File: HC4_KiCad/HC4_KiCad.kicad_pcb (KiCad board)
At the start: 2 copper layers, 150.4 x 175 mm, 168 parts, among them IC1 RAM, IC10 74HC4002, IC11 74HC161, IC12 74HC377, IC13 74HC161, IC14 74HC161, IC15 74HC161, IC16 74HC257, IC17 74HC257, IC18 74HC32, IC19 74HC74, IC2 ROM, IC20 74HC00, IC21 74HC4053, IC22 74HC04, IC23 74HC151, IC24 74HC14, IC3 74HC153, IC4 74HC153, IC5 74HC153, IC6 74HC153, IC7 74HC283, IC8 74HC257, IC9 74HC244, J1 Power, J2 CE, J3 Expantion_Connector, SW1 SW_SPDT, SW2 Bus_Open, SW3 SW_Push, SW4 SW_Push, SW5 SW_SPDT

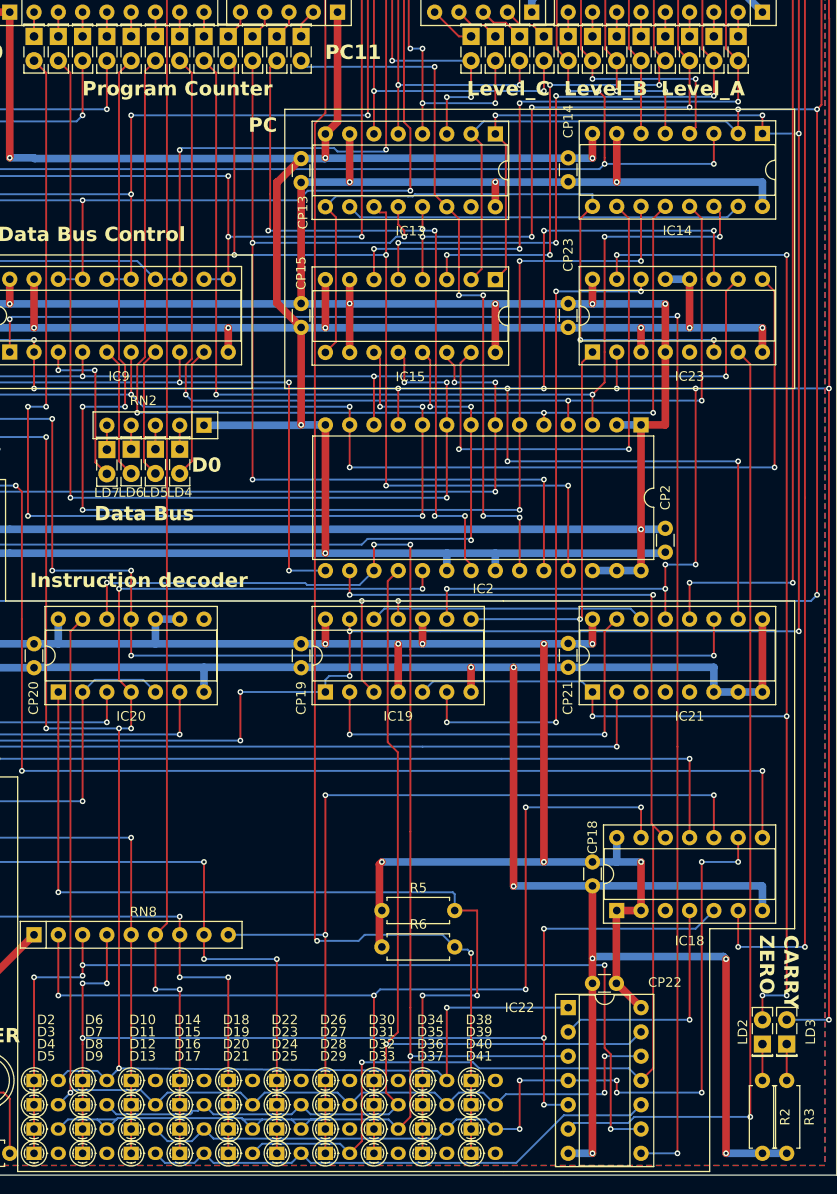
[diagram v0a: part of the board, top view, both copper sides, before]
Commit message: メモリーを外に出した　ガーバーを修正した
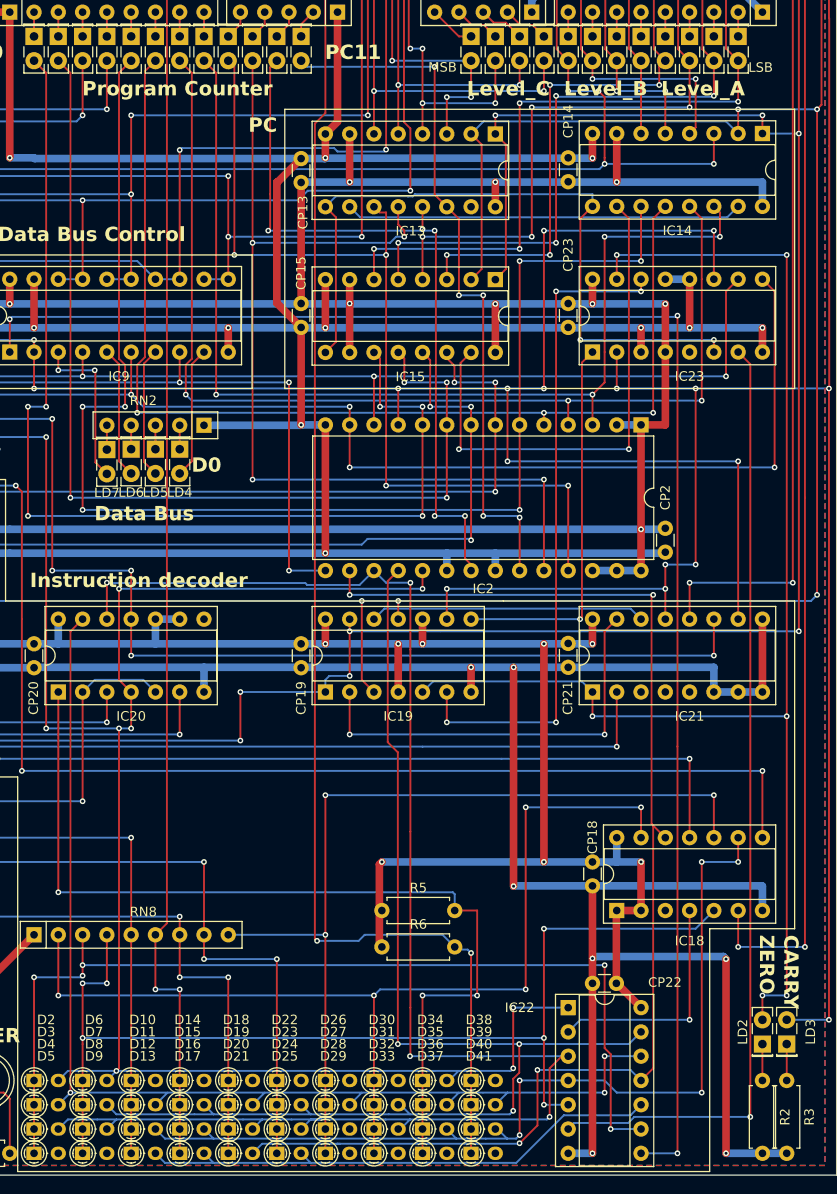
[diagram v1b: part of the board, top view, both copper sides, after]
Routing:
- net /Address BUS/Instruction_6: track 118.1 -> 131.2 mm, vias 1 -> 3
- net /Address BUS/Instruction_5: track 163.7 -> 169.4 mm
- net /Instruction Decoder/~{i6}: track 120.8 -> 124.3 mm
- net /Address BUS/Instruction_4: track 138.6 -> 136.0 mm, vias 3 -> 4
- net /Instruction Decoder/~{i5}: track 96.7 -> 98.9 mm, vias 7 -> 5
- net /Instruction Decoder/~{i4}: track 55.4 -> 56.6 mm
- net /Address BUS/Instruction_7: track 300.0 -> 300.9 mm, vias 11 -> 12
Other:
- board text added: "LSB"
- board text added: "MSB"

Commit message: 回路の改良　試験は明日やる
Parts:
- removed the IC20 at (94.0, 147.3)
- removed the RN1 at (57.2, 109.2)
- added IC21: 74HC00, Package_DIP:DIP-14_W7.62mm_Socket, F.Cu at (94.0, 147.3)
- added J2: ~{CE}_EXT, Connector_PinHeader_2.54mm:PinHeader_1x01_P2.54mm_Vertical, F.Cu at (243.3, 84.7)
- added JP1: RAM_Select, Connector_PinHeader_2.54mm:PinHeader_1x03_P2.54mm_Vertical, F.Cu at (238.6, 81.5)
- added RN2: 10k, Resistor_THT:R_Array_SIP9, F.Cu at (202.6, 84.5)
- added RN8: 1k, Resistor_THT:R_Array_SIP5, F.Cu at (252.1, 115.8)
- added SW1: SW_SPDT_312, Button_Switch_THT:SW_Slide-03_Wuerth-WS-SLTV_10x2.5x6.4_P2.54mm, F.Cu at (242.1, 77.2)
- D10, D11, D12, D13, D14, D15, D16, D17, D18, D19, D2, D20, D21, D22, D23, D24, D25, D26, D27, D28, D29, D3, D30, D31, D32, D33, D34, D35, D36, D37, D38, D39, D4, D40, D41, D5, D6, D7, D8, D9: footprint Library:DO-35_horizontal_anodeup_Smallhole -> Diode_SMD:D_SOD-323_HandSoldering
- IC1: value RAM -> KM62256CLP
- IC2: footprint Package_DIP:DIP-28_W15.24mm -> Socket:DIP_Socket-28_W11.9_W12.7_W15.24_W17.78_W18.5_3M_228-1277-00-0602J
- LD1: footprint LED_THT:LED_D5.0mm -> LED_THT:LED_Rectangular_W5.0mm_H2.0mm
- LD40, LD41: value D -> LED; footprint LED_THT:LED_D5.0mm -> LED_THT:LED_Rectangular_W5.0mm_H2.0mm
- RN3: value R_Network04_Split -> 1k; footprint Resistor_THT:R_Array_SIP5 -> Resistor_THT:R_Array_SIP9
- RN4: value R_Network08_Split -> 1k
- RN5: footprint Resistor_THT:R_Array_SIP5 -> Resistor_THT:R_Array_SIP9
- RN7: value 1k -> 10k
- moved RN7 229.4 mm to (252.1, 90.0)
- moved CP17 216.6 mm to (274.2, -4.97), turned to 0 degrees
- moved LD32 211.6 mm to (241.2, -4.71), turned to 0 degrees
- moved LD33 208.4 mm to (241.2, -1.04), turned to 0 degrees
- moved LD34 205.3 mm to (241.2, 2.62), turned to 0 degrees
- moved LD35 202.3 mm to (241.2, 6.29), turned to 0 degrees
- moved IC17 199.8 mm to (259.6, -0.07), turned to 0 degrees
- moved LD36 199.3 mm to (241.2, 9.96), turned to 0 degrees
- moved CP1 198.7 mm to (242.5, 80.8), turned to 0 degrees
- moved LD37 196.4 mm to (241.2, 13.6), turned to 0 degrees
- moved LD38 193.6 mm to (241.2, 17.3), turned to 0 degrees
- moved IC16 191.9 mm to (247.9, -0.07), turned to 0 degrees
- moved R4 191.8 mm to (258.9, 21.9), turned to 0 degrees
- moved LD39 190.8 mm to (241.2, 21.0), turned to 0 degrees
- moved LD31 185.4 mm to (276.8, 73.4), turned to 0 degrees
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- renumbered IC19 to IC18, IC18 to IC19, IC22 to IC20, IC21 to IC22, R12 to R10, R15 to R11, R9 to R7, R10 to R8, R11 to R9, RN2 to RN1
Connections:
- net /Data BUS/Stack0 renamed /Data BUS/Databus0
- net /Data BUS/Stack1 renamed /Data BUS/Databus1
- net /Data BUS/Stack2 renamed /Data BUS/Databus2
- net /Data BUS/Stack3 renamed /Data BUS/Databus3
- net /Instruction Decoder/ALU_~{Eb} renamed /Instruction Decoder/~{Carry_EN}
- D10 pad 1: /Address BUS/MEMMode -> unconnected-(D10-K-Pad1)
- D10 pad 2: unconnected-(D10-A-Pad2) -> /Address BUS/MEMMode
- D11 pad 1: /Address BUS/MEMMode -> /Instruction Decoder/~{i6}
- D11 pad 2: /Instruction Decoder/~{i6} -> /Address BUS/MEMMode
- D12 pad 1: /Address BUS/MEMMode -> /Instruction Decoder/~{i5}
- D12 pad 2: /Instruction Decoder/~{i5} -> /Address BUS/MEMMode
- D13 pad 1: /Address BUS/MEMMode -> /Instruction Decoder/~{i4}
- D13 pad 2: /Instruction Decoder/~{i4} -> /Address BUS/MEMMode
- D14 pad 1: /ALU/I0a -> unconnected-(D14-K-Pad1)
- D14 pad 2: unconnected-(D14-A-Pad2) -> /ALU/Carry_IN
- D15 pad 1: /ALU/I0a -> /Address BUS/Instruction_6
- D15 pad 2: /Address BUS/Instruction_6 -> /ALU/Carry_IN
- D16 pad 1: /ALU/I0a -> /Instruction Decoder/~{i5}
- D16 pad 2: /Instruction Decoder/~{i5} -> /ALU/Carry_IN
- D17 pad 1: /ALU/I0a -> /Instruction Decoder/~{i4}
- D17 pad 2: /Instruction Decoder/~{i4} -> /ALU/Carry_IN
- D18 pad 1: Net-(D18-K) -> unconnected-(D18-K-Pad1)
- D18 pad 2: unconnected-(D18-A-Pad2) -> Net-(D18-A)
- D19 pad 1: Net-(D18-K) -> /Instruction Decoder/~{i6}
- D19 pad 2: /Instruction Decoder/~{i6} -> Net-(D18-A)
- D2 pad 1: Net-(D2-K) -> unconnected-(D2-K-Pad1)
- D2 pad 2: /Address BUS/Instruction_7 -> Net-(D2-A)
- D20 pad 1: Net-(D18-K) -> unconnected-(D20-K-Pad1)
- D20 pad 2: /Address BUS/Instruction_5 -> Net-(D18-A)
- D21 pad 1: Net-(D18-K) -> /Address BUS/Instruction_4
- D21 pad 2: /Address BUS/Instruction_4 -> Net-(D18-A)
- D22 pad 1: Net-(D22-K) -> unconnected-(D22-K-Pad1)
- D22 pad 2: unconnected-(D22-A-Pad2) -> Net-(D22-A)
- D23 pad 1: Net-(D22-K) -> /Address BUS/Instruction_6
- D23 pad 2: /Address BUS/Instruction_6 -> Net-(D22-A)
- D24 pad 1: Net-(D22-K) -> /Address BUS/Instruction_5
- D24 pad 2: /Address BUS/Instruction_5 -> Net-(D22-A)
- D25 pad 1: Net-(D22-K) -> /Instruction Decoder/~{i4}
- D25 pad 2: /Instruction Decoder/~{i4} -> Net-(D22-A)
- D26 pad 1: Net-(D26-K) -> unconnected-(D26-K-Pad1)
- D26 pad 2: unconnected-(D26-A-Pad2) -> Net-(D26-A)
- D27 pad 1: Net-(D26-K) -> /Instruction Decoder/~{i6}
- D27 pad 2: /Instruction Decoder/~{i6} -> Net-(D26-A)
- D28 pad 1: Net-(D26-K) -> unconnected-(D28-K-Pad1)
- D28 pad 2: unconnected-(D28-A-Pad2) -> Net-(D26-A)
- D29 pad 1: Net-(D26-K) -> /Address BUS/Instruction_4
- D29 pad 2: /Address BUS/Instruction_4 -> Net-(D26-A)
- D3 pad 1: Net-(D2-K) -> /Instruction Decoder/~{i6}
- D3 pad 2: /Instruction Decoder/~{i6} -> Net-(D2-A)
- D30 pad 1: Net-(D30-K) -> unconnected-(D30-K-Pad1)
- D30 pad 2: unconnected-(D30-A-Pad2) -> Net-(D30-A)
- D31 pad 1: Net-(D30-K) -> /Address BUS/Instruction_6
- D31 pad 2: /Address BUS/Instruction_6 -> Net-(D30-A)
- D32 pad 1: Net-(D30-K) -> /Address BUS/Instruction_5
- D32 pad 2: /Address BUS/Instruction_5 -> Net-(D30-A)
- D33 pad 1: Net-(D30-K) -> unconnected-(D33-K-Pad1)
- D33 pad 2: unconnected-(D33-A-Pad2) -> Net-(D30-A)
- D34 pad 1: /Instruction Decoder/READ -> /Address BUS/Instruction_7
- D34 pad 2: /Address BUS/Instruction_7 -> /Instruction Decoder/READ
- D35 pad 1: /Instruction Decoder/READ -> /Instruction Decoder/~{i6}
- D35 pad 2: /Instruction Decoder/~{i6} -> /Instruction Decoder/READ
- D36 pad 1: /Instruction Decoder/READ -> /Instruction Decoder/~{i5}
- D36 pad 2: /Instruction Decoder/~{i5} -> /Instruction Decoder/READ
- D37 pad 1: /Instruction Decoder/READ -> unconnected-(D37-K-Pad1)
- D37 pad 2: unconnected-(D37-A-Pad2) -> /Instruction Decoder/READ
- D38 pad 1: /Data BUS/Level_C_OE -> unconnected-(D38-K-Pad1)
- D38 pad 2: unconnected-(D38-A-Pad2) -> /Data BUS/Level_C_OE
- D39 pad 1: /Data BUS/Level_C_OE -> /Instruction Decoder/~{i6}
- D39 pad 2: /Instruction Decoder/~{i6} -> /Data BUS/Level_C_OE
- D4 pad 1: Net-(D2-K) -> /Address BUS/Instruction_5
- D4 pad 2: /Address BUS/Instruction_5 -> Net-(D2-A)
- D40 pad 1: /Data BUS/Level_C_OE -> /Instruction Decoder/~{i5}
- D40 pad 2: /Instruction Decoder/~{i5} -> /Data BUS/Level_C_OE
- D41 pad 1: /Data BUS/Level_C_OE -> unconnected-(D41-K-Pad1)
- D41 pad 2: unconnected-(D41-A-Pad2) -> /Data BUS/Level_C_OE
- D5 pad 1: Net-(D2-K) -> unconnected-(D5-K-Pad1)
- D5 pad 2: unconnected-(D5-A-Pad2) -> Net-(D2-A)
- D6 pad 1: Net-(D6-K) -> /Address BUS/Instruction_7
- D6 pad 2: /Address BUS/Instruction_7 -> Net-(D6-A)
- D7 pad 1: Net-(D6-K) -> /Address BUS/Instruction_6
- D7 pad 2: /Address BUS/Instruction_6 -> Net-(D6-A)
- D8 pad 1: Net-(D6-K) -> /Address BUS/Instruction_5
- D8 pad 2: /Address BUS/Instruction_5 -> Net-(D6-A)
- D9 pad 1: Net-(D6-K) -> unconnected-(D9-K-Pad1)
- D9 pad 2: unconnected-(D9-A-Pad2) -> Net-(D6-A)
- IC1 pad 16: Net-(IC1-Q4) -> /Data BUS/Dummy4
- IC1 pad 17: Net-(IC1-Q5) -> /Data BUS/Dummy5
- IC1 pad 18: Net-(IC1-Q6) -> /Data BUS/Dummy6
- IC1 pad 19: Net-(IC1-Q7) -> /Data BUS/Dummy7
- IC10 pad 2: Net-(D18-K) -> Net-(D18-A)
- IC10 pad 3: Net-(D18-K) -> Net-(D18-A)
- IC10 pad 4: Net-(D22-K) -> Net-(D22-A)
- IC10 pad 5: Net-(D22-K) -> Net-(D22-A)
- IC13 pad 11: /Program Counter/PC_8 -> /Program Counter/PC_11
- IC13 pad 12: /Program Counter/PC_9 -> /Program Counter/PC_10
- IC13 pad 13: /Program Counter/PC_10 -> /Program Counter/PC_9
- IC13 pad 14: /Program Counter/PC_11 -> /Program Counter/PC_8
- IC13 pad 3: /Data BUS/Level_C3 -> /Data BUS/Level_C0
- IC13 pad 4: /Data BUS/Level_C2 -> /Data BUS/Level_C1
- IC13 pad 5: /Data BUS/Level_C1 -> /Data BUS/Level_C2
- IC13 pad 6: /Data BUS/Level_C0 -> /Data BUS/Level_C3
- IC14 pad 11: /Program Counter/PC_4 -> /Program Counter/PC_7
- IC14 pad 12: /Program Counter/PC_5 -> /Program Counter/PC_6
- IC14 pad 13: /Program Counter/PC_6 -> /Program Counter/PC_5
- IC14 pad 14: /Program Counter/PC_7 -> /Program Counter/PC_4
- IC14 pad 3: /ALU/ALU_in_B3 -> /ALU/ALU_in_B0
- IC14 pad 4: /ALU/ALU_in_B2 -> /ALU/ALU_in_B1
- IC14 pad 5: /ALU/ALU_in_B1 -> /ALU/ALU_in_B2
- IC14 pad 6: /ALU/ALU_in_B0 -> /ALU/ALU_in_B3
- IC15 pad 11: /Program Counter/PC_0 -> /Program Counter/PC_3
- IC15 pad 12: /Program Counter/PC_1 -> /Program Counter/PC_2
- IC15 pad 13: /Program Counter/PC_2 -> /Program Counter/PC_1
- IC15 pad 14: /Program Counter/PC_3 -> /Program Counter/PC_0
- IC15 pad 3: /ALU/ALU_in_A3 -> /ALU/ALU_in_A0
- IC15 pad 4: /ALU/ALU_in_A2 -> /ALU/ALU_in_A1
- IC15 pad 5: /ALU/ALU_in_A1 -> /ALU/ALU_in_A2
- IC15 pad 6: /ALU/ALU_in_A0 -> /ALU/ALU_in_A3
- IC19 pad 10: Net-(D26-K) -> Net-(D26-A)
- IC19 pad 13: Net-(D30-K) -> Net-(D30-A)
- IC19 pad 5: Net-(D6-K) -> Net-(D6-A)
- IC20 pad 5: Net-(D6-K) -> Net-(D6-A)
- IC20 pad 8: /Data BUS/~{Immediate_OE} -> unconnected-(IC20-Pad8)
- IC20 pad 9: Net-(D2-K) -> VCC
- IC22 pad 10: /Address BUS/Instruction_0 -> /Address BUS/Instruction_7
- IC3 pad 6: /ALU/I0a -> /ALU/Carry_IN
- IC4 pad 6: /ALU/I0a -> /ALU/Carry_IN
- IC5 pad 6: /ALU/I0a -> /ALU/Carry_IN
- IC6 pad 6: /ALU/I0a -> /ALU/Carry_IN
- IC7 pad 7: /Instruction Decoder/Carry_Flg -> /ALU/Carry_IN
- J3 pad 10: unconnected-(J3-Pin_10-Pad10) -> /Data BUS/Dummy7
- J3 pad 7: unconnected-(J3-Pin_7-Pad7) -> /Data BUS/Dummy4
- J3 pad 8: unconnected-(J3-Pin_8-Pad8) -> /Data BUS/Dummy5
- J3 pad 9: unconnected-(J3-Pin_9-Pad9) -> /Data BUS/Dummy6
- LD20 pad 2: /Program Counter/PC_11 -> /Program Counter/PC_8
- LD21 pad 2: /Program Counter/PC_7 -> /Program Counter/PC_4
- LD22 pad 2: /Program Counter/PC_3 -> /Program Counter/PC_0
- LD23 pad 2: /Program Counter/PC_10 -> /Program Counter/PC_9
- LD24 pad 2: /Program Counter/PC_6 -> /Program Counter/PC_5
- LD25 pad 2: /Program Counter/PC_2 -> /Program Counter/PC_1
- LD26 pad 2: /Program Counter/PC_9 -> /Program Counter/PC_10
- LD27 pad 2: /Program Counter/PC_5 -> /Program Counter/PC_6
- LD28 pad 2: /Program Counter/PC_1 -> /Program Counter/PC_2
- LD29 pad 2: /Program Counter/PC_8 -> /Program Counter/PC_11
- LD30 pad 2: /Program Counter/PC_4 -> /Program Counter/PC_7
- LD31 pad 2: /Program Counter/PC_0 -> /Program Counter/PC_3
- LD40 pad 2: Net-(LD40-Pad2) -> Net-(RN8C-R3.2)
- LD41 pad 2: Net-(LD41-Pad2) -> Net-(RN8D-R4.2)
- R7 pad 1: Net-(R7-Pad2) -> Net-(RN8A-R1.2)
- R8 pad 1: Net-(R10-Pad1) -> Net-(RN8B-R2.2)
- RN4 pad 6: Net-(LD15-K) -> Net-(LD20-K)
- RN4 pad 7: Net-(LD14-K) -> Net-(LD23-K)
- RN4 pad 8: Net-(LD13-K) -> Net-(LD26-K)
- RN4 pad 9: Net-(LD12-K) -> Net-(LD29-K)
- RN5 pad 2: Net-(LD20-K) -> Net-(LD21-K)
- RN5 pad 3: Net-(LD23-K) -> Net-(LD24-K)
- RN5 pad 4: Net-(LD26-K) -> Net-(LD27-K)
- RN5 pad 5: Net-(LD29-K) -> Net-(LD30-K)
- RN6 pad 2: Net-(LD31-K) -> Net-(LD32-K)
- RN6 pad 3: Net-(LD28-K) -> Net-(LD33-K)
- RN6 pad 4: Net-(LD25-K) -> Net-(LD34-K)
- RN6 pad 5: Net-(LD22-K) -> Net-(LD35-K)
- RN6 pad 6: Net-(LD30-K) -> Net-(LD36-K)
- RN6 pad 7: Net-(LD27-K) -> Net-(LD37-K)
- RN6 pad 8: Net-(LD24-K) -> Net-(LD38-K)
- RN6 pad 9: Net-(LD21-K) -> Net-(LD39-K)
- RN7 pad 1: GND -> VCC
- RN7 pad 2: Net-(LD32-K) -> Net-(D2-A)
- RN7 pad 3: Net-(LD33-K) -> Net-(D6-A)
- RN7 pad 4: Net-(LD34-K) -> /Address BUS/MEMMode
- RN7 pad 5: Net-(LD35-K) -> /ALU/Carry_IN
- RN7 pad 6: Net-(LD36-K) -> Net-(D18-A)
- RN7 pad 7: Net-(LD37-K) -> Net-(D22-A)
- RN7 pad 8: Net-(LD38-K) -> Net-(D26-A)
- RN7 pad 9: Net-(LD39-K) -> Net-(D30-A)
- RN8 pad 2: Net-(D30-K) -> Net-(D30-A)
- RN8 pad 3: Net-(D2-K) -> Net-(D2-A)
- RN8 pad 4: Net-(D6-K) -> Net-(D6-A)
- RN8 pad 7: Net-(D18-K) -> Net-(D18-A)
- RN8 pad 8: Net-(D22-K) -> Net-(D22-A)
- RN8 pad 9: Net-(D26-K) -> Net-(D26-A)
- SW3 pad 2: Net-(R7-Pad2) -> Net-(RN8A-R1.2)
- SW4 pad 2: Net-(R10-Pad1) -> Net-(RN8B-R2.2)
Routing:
- net GND: track 1630.3 -> 1131.1 mm, vias 43 -> 23
- net VCC: track 1368.7 -> 954.1 mm, vias 30 -> 18
- net /ALU/ALU_in_A3: track 236.9 -> 37.0 mm, vias 13 -> 0
- net /ALU/ALU_in_A2: track 220.3 -> 33.0 mm, vias 12 -> 0
- net /ALU/ALU_in_A1: track 230.4 -> 48.6 mm, vias 14 -> 2
- net /ALU/ALU_in_B2: track 187.1 -> 10.8 mm, vias 12 -> 0
- net /ALU/ALU_in_B3: track 286.8 -> 123.7 mm, vias 13 -> 2
- net /ALU/ALU_in_B0: track 162.7 -> 10.8 mm, vias 11 -> 0
- net /ALU/ALU_in_B1: track 161.9 -> 10.8 mm, vias 9 -> 0
- net /Program Counter/PC_2: track 149.4 -> 0.00 mm, vias 6 -> 0
- net /Program Counter/PC_3: track 135.8 -> 0.00 mm, vias 6 -> 0
- net /ALU/ALU_in_A0: track 259.8 -> 136.3 mm, vias 10 -> 4
- net Net-(D6-A): track 0.00 -> 114.5 mm, vias 0 -> 6
- net /Instruction Decoder/Carry_Flg: track 302.1 -> 188.5 mm, vias 10 -> 8
- net Net-(D6-K): track 113.2 -> 0.00 mm, vias 6 -> 0
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- removed copper zone on B.Cu, net GND
- removed copper zone on F.Cu, net GND
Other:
- board text removed: "A0"
- board text removed: "A7"
- board text removed: "ALU"
- board text removed: "Address Bus"
- board text removed: "LSB"
- board text removed: "MSB"
- board text removed: "PC0"
- board text removed: "PC11"
- board text removed: "Stack Unit"

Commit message: 基板ぬ
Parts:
- removed G***: LOGO, LOGO
- removed the J2 at (35.6, 132.1)
- removed the J2 at (243.3, 84.7)
- removed the JP1 at (238.6, 81.5)
- removed the JP1 at (57.2, 104.1)
- removed the R7 at (66.9, 180.3)
- removed the R7 at (71.8, 183.5)
- removed the R8 at (77.5, 183.5)
- removed the R8 at (80.0, 183.5)
- removed RN8: 10k, Resistor_THT:R_Array_SIP9
- removed RN8: 1k, Resistor_THT:R_Array_SIP5
- removed the SW1 at (242.1, 77.2)
- removed the SW1 at (33.0, 128.3)
- added J2: ~{CE}_EXT, Connector_PinHeader_2.54mm:PinHeader_1x01_P2.54mm_Vertical, F.Cu at (213.4, 104.0)
- added JP1: RAM_Select, Connector_PinHeader_2.54mm:PinHeader_1x03_P2.54mm_Vertical, F.Cu at (213.6, 46.9)
- added R12: 10k, Resistor_SMD:R_0603_1608Metric, F.Cu at (253.4, 100.7)
- added R15: 10k, Resistor_SMD:R_0603_1608Metric, F.Cu at (285.5, 74.7)
- added R16: 100k, Resistor_SMD:R_0603_1608Metric, F.Cu at (285.5, 77.2)
- added R17: Socket, Resistor_THT:R_Axial_DIN0207_L6.3mm_D2.5mm_P10.16mm_Horizontal, F.Cu at (278.4, 90.4)
- added R18: 100, Resistor_SMD:R_0603_1608Metric, F.Cu at (285.5, 79.7)
- added R19: 100, Resistor_SMD:R_0603_1608Metric, F.Cu at (285.5, 82.2)
- added R7: 10k, Resistor_SMD:R_0603_1608Metric, F.Cu at (249.4, 103.2)
- added R8: 10k, Resistor_SMD:R_0603_1608Metric, F.Cu at (249.4, 105.7)
- added REF**: MountingHole_3.2mm_M3, MountingHole:MountingHole_3.2mm_M3, F.Cu at (54.0, 146.1)
- added REF**: MountingHole_3.2mm_M3, MountingHole:MountingHole_3.2mm_M3, F.Cu at (146.1, 146.1)
- added REF**: MountingHole_3.2mm_M3, MountingHole:MountingHole_3.2mm_M3, F.Cu at (54.0, 57.8)
- added SW1: SW_SPDT_312, Button_Switch_THT:SW_Slide-03_Wuerth-WS-SLTV_10x2.5x6.4_P2.54mm, F.Cu at (198.7, 100.5)
- CP1, CP10, CP11, CP12, CP13, CP14, CP15, CP16, CP17, CP18, CP19, CP2, CP20, CP21, CP22, CP23, CP24, CP3, CP4, CP5, CP6, CP7, CP8, CP9: footprint Capacitor_THT:C_Disc_D3.0mm_W1.6mm_P2.50mm -> Capacitor_SMD:C_0603_1608Metric
- IC1: footprint Package_DIP:DIP-28_W15.24mm -> Package_SO:SOP-28_8.4x18.16mm_P1.27mm
- IC10, IC18, IC19, IC20, IC21, IC24: footprint Package_DIP:DIP-14_W7.62mm_Socket -> Package_SO:SO-14_5.3x10.2mm_P1.27mm
- IC11, IC13, IC14, IC15, IC16, IC17, IC22, IC23, IC3, IC4, IC5, IC6, IC7, IC8: footprint Package_DIP:DIP-16_W7.62mm_Socket -> Package_SO:SO-16_5.3x10.2mm_P1.27mm
- IC12, IC9: footprint Package_DIP:DIP-20_W7.62mm_Socket -> Package_SO:SOP-20_7.5x12.8mm_P1.27mm
- R1, R2, R3, R4, R5, R6: footprint Resistor_THT:R_Axial_DIN0207_L6.3mm_D2.5mm_P7.62mm_Horizontal -> Resistor_SMD:R_0603_1608Metric
- R10, R11: value 100 -> 10k; footprint Resistor_THT:R_Axial_DIN0207_L6.3mm_D2.5mm_P7.62mm_Horizontal -> Resistor_SMD:R_0603_1608Metric
- R13, R14: value 1k -> 10k; footprint Resistor_THT:R_Axial_DIN0207_L6.3mm_D2.5mm_P7.62mm_Horizontal -> Resistor_SMD:R_0603_1608Metric
- R9: value Socket -> 10k; footprint Resistor_THT:R_Axial_DIN0207_L6.3mm_D2.5mm_P7.62mm_Horizontal -> Resistor_SMD:R_0603_1608Metric
- RN7: value 10k -> 1k; footprint Resistor_THT:R_Array_SIP9 -> Resistor_THT:R_Array_SIP5
- moved CP24 261.0 mm to (285.5, 72.2), turned to 0 degrees
- moved LD41 253.9 mm to (289.6, 76.4), turned to 0 degrees
- moved LD40 252.9 mm to (289.6, 72.8), turned to 0 degrees
- moved C4 251.7 mm to (290.7, 95.7)
- moved IC24 239.4 mm to (271.5, 93.9), turned to 0 degrees
- moved C2 229.8 mm to (279.0, 74.2), turned to 0 degrees
- moved C3 229.7 mm to (279.0, 80.7), turned to 0 degrees
- moved R14 226.8 mm to (253.4, 105.7)
- moved R13 225.9 mm to (253.4, 103.2)
- moved R9 219.7 mm to (249.4, 108.2)
- moved SW5 216.5 mm to (282.6, 94.4)
- moved RN6 202.7 mm to (53.3, 52.1)
- moved R11 202.3 mm to (253.4, 98.2), turned to 0 degrees
- moved LD32 192.8 mm to (59.1, 58.4), turned to -90 degrees
- moved IC16 191.8 mm to (68.6, 67.9), turned to 90 degrees
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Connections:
- IC21 pad 4: /Address BUS/Instruction_7 -> /Instruction Decoder/~{i7}
- LD40 pad 2: Net-(RN8C-R3.2) -> Net-(RN7C-R3.2)
- LD41 pad 2: Net-(RN8D-R4.2) -> Net-(RN7D-R4.2)
- R10 pad 1: Net-(SW5-B) -> VCC
- R10 pad 2: CLK2 -> Net-(D22-A)
- R11 pad 1: Net-(IC24-Pad12) -> VCC
- R11 pad 2: CLK -> Net-(D26-A)
- R13 pad 2: Net-(LD40-Pad2) -> /Instruction Decoder/READ
- R14 pad 2: Net-(LD41-Pad2) -> /Data BUS/Level_C_OE
- R5 pad 2: /Instruction Decoder/READ -> Net-(D2-A)
- R6 pad 2: /Data BUS/Level_C_OE -> Net-(D6-A)
- R9 pad 1: Net-(C4-Pad1) -> VCC
- R9 pad 2: Net-(IC24-Pad2) -> Net-(D18-A)
- RN3 pad 2: Net-(LD11-K) -> Net-(LD8-K)
- RN3 pad 3: Net-(LD10-K) -> Net-(LD9-K)
- RN3 pad 4: Net-(LD9-K) -> Net-(LD10-K)
- RN3 pad 5: Net-(LD8-K) -> Net-(LD11-K)
- RN3 pad 6: Net-(LD15-K) -> Net-(LD12-K)
- RN3 pad 7: Net-(LD14-K) -> Net-(LD13-K)
- RN3 pad 8: Net-(LD13-K) -> Net-(LD14-K)
- RN3 pad 9: Net-(LD12-K) -> Net-(LD15-K)
- RN4 pad 2: Net-(LD19-K) -> Net-(LD16-K)
- RN4 pad 3: Net-(LD18-K) -> Net-(LD17-K)
- RN4 pad 4: Net-(LD17-K) -> Net-(LD18-K)
- RN4 pad 5: Net-(LD16-K) -> Net-(LD19-K)
- RN4 pad 6: Net-(LD20-K) -> Net-(LD29-K)
- RN4 pad 7: Net-(LD23-K) -> Net-(LD26-K)
- RN4 pad 8: Net-(LD26-K) -> Net-(LD23-K)
- RN4 pad 9: Net-(LD29-K) -> Net-(LD20-K)
- RN5 pad 2: Net-(LD21-K) -> Net-(LD30-K)
- RN5 pad 3: Net-(LD24-K) -> Net-(LD27-K)
- RN5 pad 4: Net-(LD27-K) -> Net-(LD24-K)
- RN5 pad 5: Net-(LD30-K) -> Net-(LD21-K)
- RN5 pad 6: Net-(LD22-K) -> Net-(LD31-K)
- RN5 pad 7: Net-(LD25-K) -> Net-(LD28-K)
- RN5 pad 8: Net-(LD28-K) -> Net-(LD25-K)
- RN5 pad 9: Net-(LD31-K) -> Net-(LD22-K)
- RN7 pad 2: Net-(D2-A) -> Net-(RN7A-R1.2)
- RN7 pad 3: Net-(D6-A) -> Net-(RN7B-R2.2)
- RN7 pad 4: /Address BUS/MEMMode -> Net-(RN7C-R3.2)
- RN7 pad 5: /ALU/Carry_IN -> Net-(RN7D-R4.2)
- SW3 pad 2: Net-(RN8A-R1.2) -> Net-(RN7A-R1.2)
- SW4 pad 2: Net-(RN8B-R2.2) -> Net-(RN7B-R2.2)
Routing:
- net GND: track 1131.1 -> 9.00 mm, vias 23 -> 0
- net VCC: track 954.1 -> 4.52 mm, vias 18 -> 0
- net ~{RESET}: track 456.8 -> 0.00 mm, vias 11 -> 0
- net CLK: track 287.1 -> 0.00 mm, vias 5 -> 0
- net /Address BUS/Instruction_0: track 273.0 -> 0.00 mm, vias 10 -> 0
- net /Address BUS/Instruction_7: track 245.3 -> 0.00 mm, vias 11 -> 0
- net /Data BUS/Databus2: track 201.9 -> 0.00 mm, vias 8 -> 0
- net /Instruction Decoder/Carry_Flg: track 188.5 -> 0.00 mm, vias 8 -> 0
- net CLK2: track 187.9 -> 0.00 mm, vias 5 -> 0
- net /Address BUS/Instruction_2: track 182.7 -> 0.00 mm, vias 5 -> 0
- net /Address BUS/MEMMode: track 181.6 -> 0.00 mm, vias 2 -> 0
- net /Address BUS/Instruction_1: track 181.5 -> 0.00 mm, vias 4 -> 0
- net /Data BUS/Databus0: track 177.7 -> 0.00 mm, vias 5 -> 0
- net /Data BUS/Databus1: track 172.9 -> 0.00 mm, vias 6 -> 0
- net /ALU/I2a: track 172.3 -> 0.00 mm, vias 4 -> 0
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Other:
- board size 150.4 x 175 mm -> 100 x 100 mm
- board text removed: "CARRY"
- board text removed: "CLOCK"
- board text removed: "Clock and Reset"
- board text removed: "D0"
- board text removed: "Data Bus"
- board text removed: "Data Bus Control"
- board text removed: "Designed and assenbled in Japan 2509 DGK"
- board text removed: "Expantion Connector"
- board text removed: "HC4_CPU Rev 1.2"
- board text removed: "Instruction decoder"
- board text removed: "Level_A"
- board text removed: "Level_B"
- board text removed: "Level_C"
- board text removed: "PC"
- board text removed: "POWER"
- board text removed: "RESET"
- board text removed: "ZERO"
